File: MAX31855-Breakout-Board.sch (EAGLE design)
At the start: 5 parts, among them U1 MAX6675MAX31855

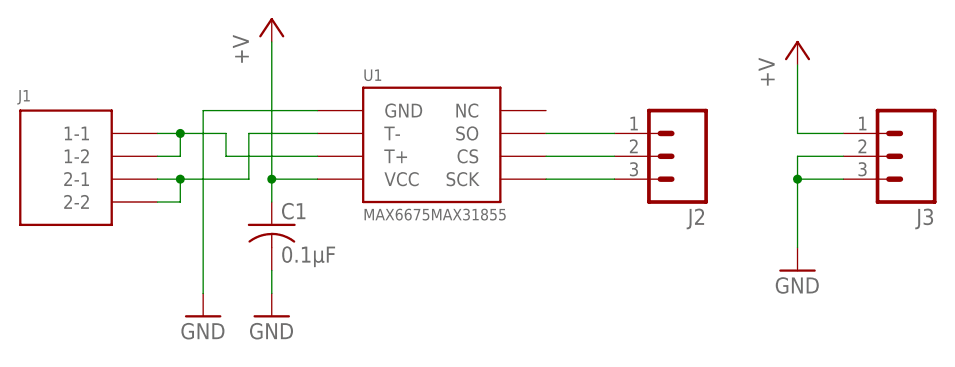
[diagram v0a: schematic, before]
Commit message: Updated to use screw terminal header and updated for v1.1 and 01-2012 production
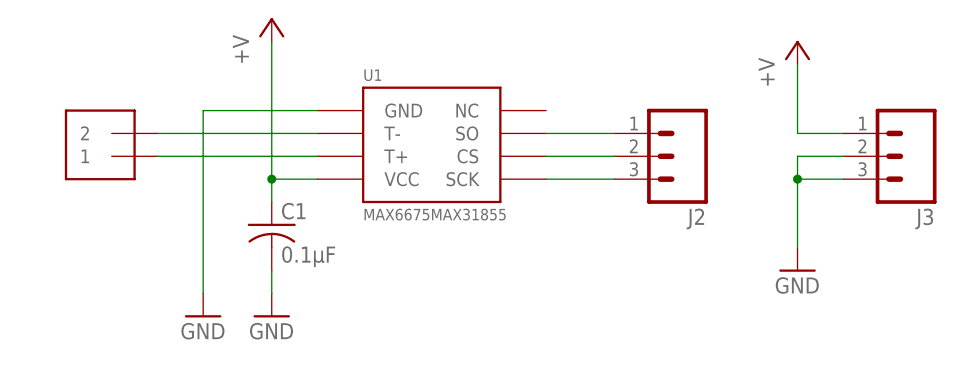
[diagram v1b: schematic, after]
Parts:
- removed J1: (no value), McLEng:WIRE-TO-BOARD_2PIN_SMD
- added J4: 1X2-3.5MM, adafruit:1X2-3.5MM
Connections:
- removed net N$1: J1.2-1, J1.2-2, U1.T-
- removed net N$2: J1.1-1, J1.1-2, U1.T+
- new net T+: J4.1, U1.T+
- new net T-: J4.2, U1.T-
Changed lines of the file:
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@@
 <layer number="106" name="bPlate" color="7" fill="1" visible="yes" active="yes"/>
 <layer number="107" name="Crop" color="7" fill="1" visible="yes" active="yes"/>
+<layer number="108" name="fp8" color="7" fill="1" visible="no" active="yes"/>
+<layer number="109" name="fp9" color="7" fill="1" visible="no" active="yes"/>
+<layer number="110" name="fp0" color="7" fill="1" visible="no" active="yes"/>
+<layer number="111" name="LPC17xx" color="7" fill="1" visible="yes" active="yes"/>
+<layer number="112" name="tSilk" color="7" fill="1" visible="yes" active="yes"/>
 <layer number="116" name="Patch_BOT" color="9" fill="4" visible="yes" active="yes"/>
 <layer number="121" name="_tsilk" color="7" fill="1" visible="yes" active="yes"/>
 <layer number="122" name="_bsilk" color="7" fill="1" visible="yes" active="yes"/>
+<layer number="123" name="tTestmark" color="7" fill="1" visible="no" active="yes"/>
+<layer number="124" name="bTestmark" color="7" fill="1" visible="no" active="yes"/>
+<layer number="125" name="_tNames" color="7" fill="1" visible="yes" active="yes"/>
+<layer number="126" name="_bNames" color="7" fill="1" visible="yes" active="yes"/>
+<layer number="127" name="_tValues" color="7" fill="1" visible="yes" active="yes"/>
+<layer number="128" name="_bValues" color="7" fill="1" visible="yes" active="yes"/>
+<layer number="131" name="tAdjust" color="7" fill="1" visible="no" active="yes"/>
+<layer number="132" name="bAdjust" color="7" fill="1" visible="no" active="yes"/>
 <layer number="144" name="Drill_legend" color="7" fill="1" visible="yes" active="yes"/>
 <layer number="151" name="HeatSink" color="7" fill="1" visible="yes" active="yes"/>
+<layer number="152" name="_bDocu" color="7" fill="1" visible="yes" active="yes"/>
+<layer number="199" name="Contour" color="7" fill="1" visible="yes" active="yes"/>
 <layer number="200" name="200bmp" color="1" fill="10" visible="no" active="no"/>
 <layer number="201" name="201bmp" color="2" fill="1" visible="no" active="no"/>
@@
 <layer number="215" name="215bmp" color="7" fill="1" visible="yes" active="yes"/>
 <layer number="216" name="216bmp" color="7" fill="1" visible="yes" active="yes"/>
+<layer number="217" name="217bmp" color="18" fill="1" visible="no" active="no"/>
+<layer number="218" name="218bmp" color="19" fill="1" visible="no" active="no"/>
+<layer number="219" name="219bmp" color="20" fill="1" visible="no" active="no"/>
+<layer number="220" name="220bmp" color="21" fill="1" visible="no" active="no"/>
+<layer number="221" name="221bmp" color="22" fill="1" visible="no" active="no"/>
+<layer number="222" name="222bmp" color="23" fill="1" visible="no" active="no"/>
+<layer number="223" name="223bmp" color="24" fill="1" visible="no" active="no"/>
+<layer number="224" name="224bmp" color="25" fill="1" visible="no" active="no"/>
+<layer number="248" name="Housing" color="7" fill="1" visible="yes" active="yes"/>
+<layer number="249" name="Edge" color="7" fill="1" visible="yes" active="yes"/>
 <layer number="250" name="Descript" color="3" fill="1" visible="no" active="no"/>
 <layer number="251" name="SMDround" color="12" fill="11" visible="no" active="no"/>
@@
 <part name="J2" library="SparkFun" deviceset="M03" device="1X03_NO_SILK"/>
 <part name="J3" library="SparkFun" deviceset="M03" device="1X03_NO_SILK"/>
-<part name="J1" library="McLEng" deviceset="WIRE-TO-BOARD_2PIN_SMD" device=""/>
+<part name="J4" library="adafruit" deviceset="1X2" device="-3.5MM"/>
 </parts>
 <sheets>
@@
 <instance part="J2" gate="G$1" x="88.9" y="71.12" rot="R180"/>
 <instance part="J3" gate="G$1" x="114.3" y="71.12" rot="R180"/>
-<instance part="J1" gate="G$1" x="15.24" y="63.5"/>
+<instance part="J4" gate="G$1" x="25.4" y="73.66" rot="R180"/>
 </instances>
 <busses>
@@
 </segment>
 </net>
-<net name="N$1" class="0">
+<net name="T+" class="0">
 <segment>
-<wire x1="30.48" y1="68.58" x2="33.02" y2="68.58" width="0.1524" layer="91"/>
-<wire x1="33.02" y1="68.58" x2="40.64" y2="68.58" width="0.1524" layer="91"/>
-<wire x1="40.64" y1="68.58" x2="40.64" y2="73.66" width="0.1524" layer="91"/>
-<wire x1="40.64" y1="73.66" x2="48.26" y2="73.66" width="0.1524" layer="91"/>
-<wire x1="30.48" y1="66.04" x2="33.02" y2="66.04" width="0.1524" layer="91"/>
-<wire x1="33.02" y1="66.04" x2="33.02" y2="68.58" width="0.1524" layer="91"/>
-<junction x="33.02" y="68.58"/>
-<pinref part="J1" gate="G$1" pin="2-1"/>
-<pinref part="U1" gate="G$1" pin="T-"/>
-<pinref part="J1" gate="G$1" pin="2-2"/>
+<pinref part="J4" gate="G$1" pin="1"/>
+<pinref part="U1" gate="G$1" pin="T+"/>
+<wire x1="30.48" y1="71.12" x2="48.26" y2="71.12" width="0.1524" layer="91"/>
 </segment>
 </net>
-<net name="N$2" class="0">
+<net name="T-" class="0">
 <segment>
-<wire x1="30.48" y1="73.66" x2="33.02" y2="73.66" width="0.1524" layer="91"/>
-<wire x1="33.02" y1="73.66" x2="38.1" y2="73.66" width="0.1524" layer="91"/>
-<wire x1="38.1" y1="73.66" x2="38.1" y2="71.12" width="0.1524" layer="91"/>
-<wire x1="38.1" y1="71.12" x2="48.26" y2="71.12" width="0.1524" layer="91"/>
-<wire x1="30.48" y1="71.12" x2="33.02" y2="71.12" width="0.1524" layer="91"/>
-<wire x1="33.02" y1="71.12" x2="33.02" y2="73.66" width="0.1524" layer="91"/>
-<junction x="33.02" y="73.66"/>
-<pinref part="J1" gate="G$1" pin="1-1"/>
-<pinref part="U1" gate="G$1" pin="T+"/>
-<pinref part="J1" gate="G$1" pin="1-2"/>
+<pinref part="J4" gate="G$1" pin="2"/>
+<pinref part="U1" gate="G$1" pin="T-"/>
+<wire x1="30.48" y1="73.66" x2="48.26" y2="73.66" width="0.1524" layer="91"/>
 </segment>
 </net>
